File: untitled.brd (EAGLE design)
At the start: 43.2 x 14.4 mm, 38 parts, among them J2 1x3 RA Female .1", J3 CORTEX_DEBUG_PTH

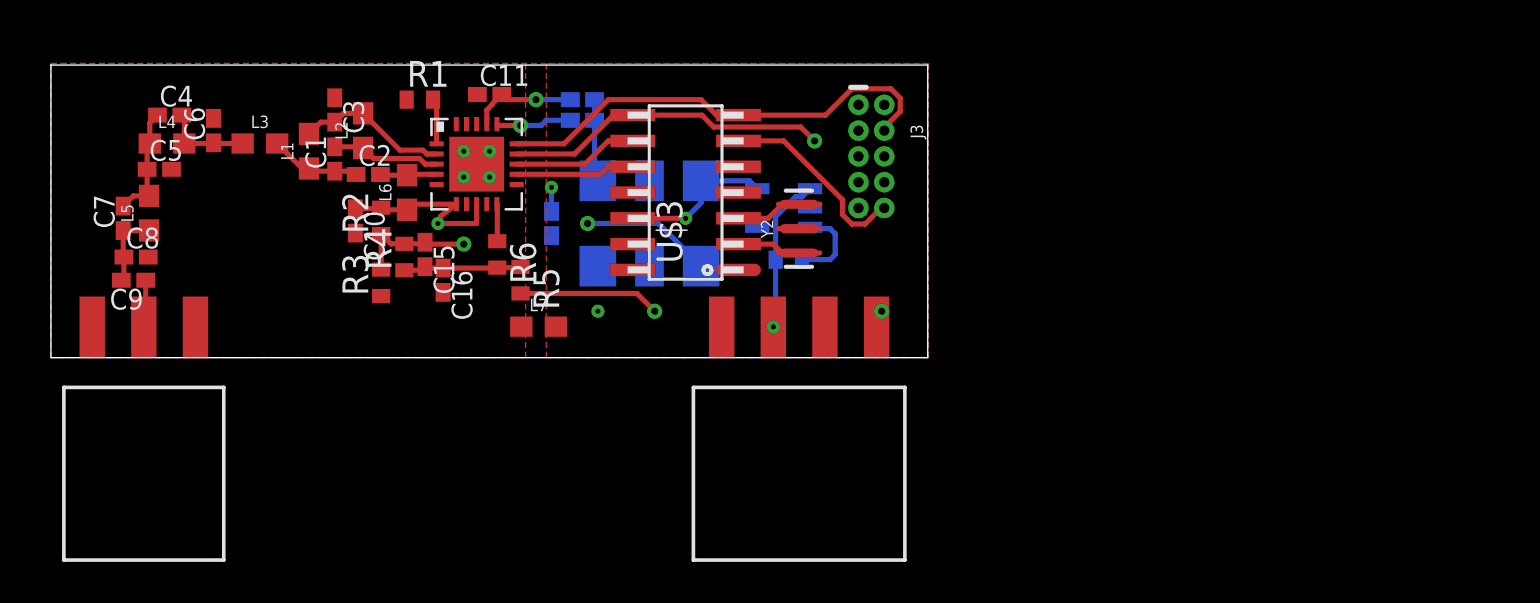
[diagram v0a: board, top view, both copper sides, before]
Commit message: Added USB connector
added USB connector for debugging, dropped to 4 layer board
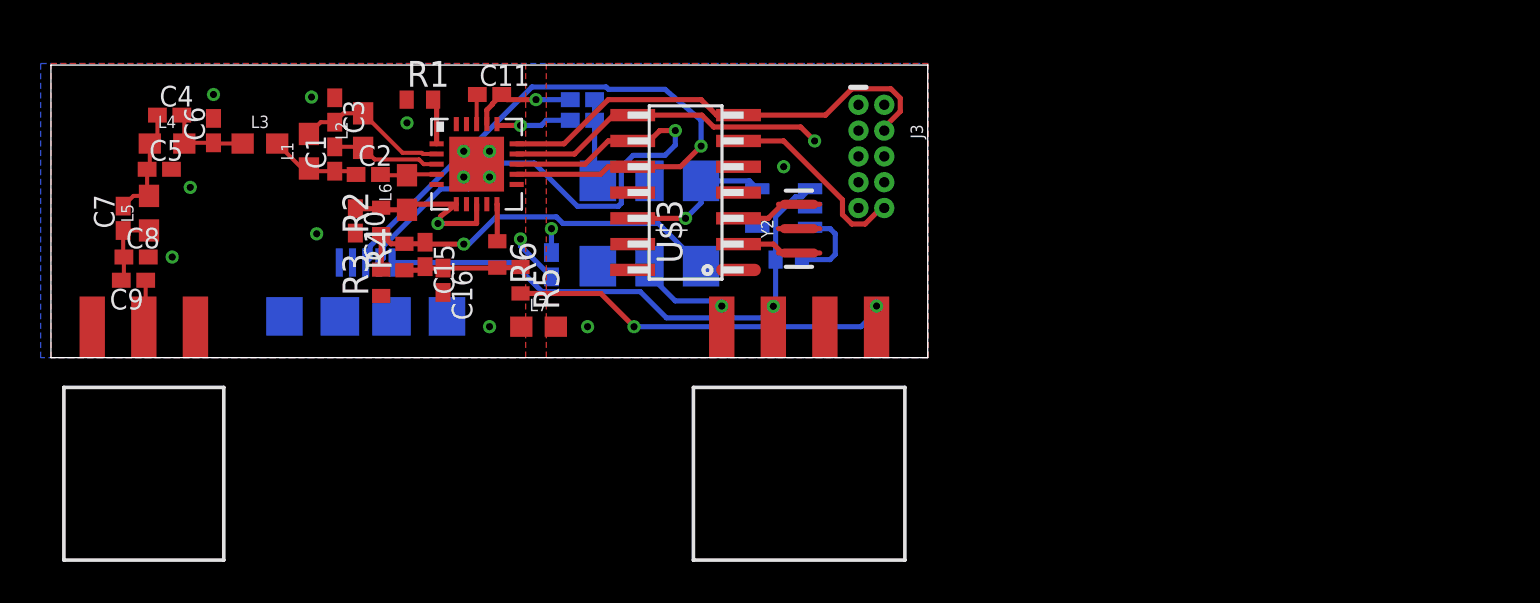
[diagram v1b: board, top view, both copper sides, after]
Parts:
- added J4: USB-MICROB, SparkFun-Retired:USB-MICROB
- moved C14 2.03 mm to (24.6, 4.57)
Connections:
- net 5V: now also J4.VBUS
- net GND: now also J4.GND, J4.MT1, J4.MT2
- net PA24: now also J4.D-
- net PA25: now also J4.D+
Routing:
- net PA25: track 5.87 -> 32.3 mm, vias 0 -> 1
- net PA24: track 6.19 -> 29.8 mm, vias 0 -> 1
- net 5V: track 8.62 -> 28.7 mm
- net ENABLE: track 0.00 -> 5.66 mm, vias 0 -> 1
- net GND: track 0.00 -> 4.87 mm, vias 5 -> 13
- net AUDIO: track 20.7 -> 19.8 mm
- net N$6: track 19.1 -> 19.3 mm, vias 2 -> 1
- net VCC: vias 3 -> 4
- added copper zone on layer 15, net VCC
- removed copper zone on layer 14, net VCC

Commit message: Added test points to SI4464
Added test points to unused pins for later use. Cleaned up routing.
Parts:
- added TP1, TP2, TP3, TP4, TP5: TEST-POINT3, SparkFun-Connectors:PAD.03X.03
- C1: value (none) -> 12pf
- C2: value (none) -> 470pf
- moved R6 1.27 mm to (22.0, 3.81)
- moved C11 0.76 mm to (22.4, 13.0)
- moved R1 0.65 mm to (17.5, 12.6), turned to 270 degrees
- moved R5 0.25 mm to (23.4, 3.81)
- moved L2 0.13 mm to (15.5, 11.2)
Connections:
- net GPIO0: now also TP2.P$1
- net GPIO2: now also TP4.P$1
- net GPIO3: now also TP5.P$1
- net NIRQ: now also TP3.P$1
- net TXRAMP: now also TP1.P$1
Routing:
- net GPIO0: track 0.00 -> 2.73 mm
- net NIRQ: track 0.00 -> 2.39 mm
- net N$6: track 19.3 -> 21.5 mm
- net GPIO3: track 0.00 -> 2.09 mm
- net 5V: track 28.7 -> 30.5 mm
- net N$4: track 5.84 -> 7.35 mm
- net GPIO2: track 0.00 -> 1.44 mm
- net MODULATION: track 1.83 -> 3.10 mm
- net TXRAMP: track 0.00 -> 1.26 mm
- net VCC: track 18.2 -> 19.2 mm
- net GND: track 4.87 -> 5.62 mm, vias 13 -> 12

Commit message: Added 0 ohm resistors to spi
added 0 ohm jumpers between spi pins on the micro and si4464
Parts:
- added R10, R11, R8, R9: 0, resistor:R0402
- moved TP3 2.17 mm to (25.9, 6.10)
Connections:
- new net PA241: R10.1, U$2.13
- new net PA251: R11.1, U$2.12
- new net SWDCLK1: R8.1, U$2.15
- new net SWDIO1: R9.1, U$2.14
- net PA24: now also R10.2; no longer U$2.13
- net PA25: now also R11.2; no longer U$2.12
- net SWDCLK: now also R8.2; no longer U$2.15
- net SWDIO: now also R9.2; no longer U$2.14
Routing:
- net SWDCLK: track 22.7 -> 19.1 mm
- net SWDIO: track 21.2 -> 17.9 mm
- net PA24: track 29.8 -> 26.9 mm
- net PA25: track 32.3 -> 29.8 mm
- net SWDCLK1: track 0.00 -> 2.31 mm
- net PA251: track 0.00 -> 2.30 mm
- net SWDIO1: track 0.00 -> 1.99 mm
- net PA241: track 0.00 -> 1.98 mm
- net NIRQ: track 2.39 -> 4.26 mm
- net VCC: vias 4 -> 3
- net GND: vias 12 -> 13
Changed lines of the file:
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@@
 <element name="TP1" library="SparkFun-Connectors" library_urn="urn:adsk.eagle:library:513" package="PAD.03X.03" package3d_urn="urn:adsk.eagle:package:38286/1" value="TEST-POINT3" x="20.32" y="6.35"/>
 <element name="TP2" library="SparkFun-Connectors" library_urn="urn:adsk.eagle:library:513" package="PAD.03X.03" package3d_urn="urn:adsk.eagle:package:38286/1" value="TEST-POINT3" x="20.828" y="5.08"/>
-<element name="TP3" library="SparkFun-Connectors" library_urn="urn:adsk.eagle:library:513" package="PAD.03X.03" package3d_urn="urn:adsk.eagle:package:38286/1" value="TEST-POINT3" x="25.146" y="8.128"/>
+<element name="TP3" library="SparkFun-Connectors" library_urn="urn:adsk.eagle:library:513" package="PAD.03X.03" package3d_urn="urn:adsk.eagle:package:38286/1" value="TEST-POINT3" x="25.908" y="6.096"/>
 <element name="TP4" library="SparkFun-Connectors" library_urn="urn:adsk.eagle:library:513" package="PAD.03X.03" package3d_urn="urn:adsk.eagle:package:38286/1" value="TEST-POINT3" x="20.193" y="12.827"/>
 <element name="TP5" library="SparkFun-Connectors" library_urn="urn:adsk.eagle:library:513" package="PAD.03X.03" package3d_urn="urn:adsk.eagle:package:38286/1" value="TEST-POINT3" x="19.05" y="13.208"/>
+<element name="R8" library="resistor" library_urn="urn:adsk.eagle:library:348" package="R0402" package3d_urn="urn:adsk.eagle:package:26058/1" value="0" x="25.4" y="11.684"/>
+<element name="R9" library="resistor" library_urn="urn:adsk.eagle:library:348" package="R0402" package3d_urn="urn:adsk.eagle:package:26058/1" value="0" x="25.4" y="10.414"/>
+<element name="R10" library="resistor" library_urn="urn:adsk.eagle:library:348" package="R0402" package3d_urn="urn:adsk.eagle:package:26058/1" value="0" x="25.4" y="9.144"/>
+<element name="R11" library="resistor" library_urn="urn:adsk.eagle:library:348" package="R0402" package3d_urn="urn:adsk.eagle:package:26058/1" value="0" x="25.4" y="7.874"/>
 </elements>
 <signals>
@@
 <wire x1="23.114" y1="5.496" x2="23.114" y2="5.842" width="0.254" layer="16"/>
 <wire x1="20.955" y1="9.525" x2="21.59" y2="8.89" width="0.254" layer="1"/>
+<via x="38.1" y="2.54" extent="1-16" drill="0.35" diameter="0.55"/>
 </signal>
 <signal name="RADIO_SDN">
@@
 <vertex x="0" y="0"/>
 </polygon>
-<via x="36.068" y="9.398" extent="1-16" drill="0.35"/>
 <wire x1="19.955" y1="7.555" x2="19.955" y2="7.509" width="0.254" layer="1"/>
 <wire x1="19.955" y1="7.509" x2="19.05" y2="6.604" width="0.254" layer="1"/>
@@
 <contactref element="U$2" pad="11"/>
 <contactref element="TP3" pad="P$1"/>
-<wire x1="22.925" y1="8.525" x2="24.749" y2="8.525" width="0.254" layer="1"/>
-<wire x1="24.749" y1="8.525" x2="25.146" y2="8.128" width="0.254" layer="1"/>
+<wire x1="22.925" y1="8.525" x2="23.876" y2="7.574" width="0.254" layer="1"/>
+<wire x1="23.876" y1="7.574" x2="23.876" y2="7.112" width="0.254" layer="1"/>
+<wire x1="23.876" y1="7.112" x2="24.0566" y2="6.9314" width="0.254" layer="1"/>
+<wire x1="25.714225" y1="6.096" x2="25.908" y2="6.096" width="0.254" layer="1"/>
+<wire x1="24.0566" y1="6.9314" x2="24.878825" y2="6.9314" width="0.254" layer="1"/>
+<wire x1="24.878825" y1="6.9314" x2="25.714225" y2="6.096" width="0.254" layer="1"/>
 </signal>
 <signal name="TXRAMP">
@@
 <contactref element="J3" pad="2"/>
 <contactref element="U$3" pad="8"/>
-<contactref element="U$2" pad="14"/>
-<wire x1="22.925" y1="10.025" x2="25.773" y2="10.025" width="0.254" layer="1"/>
-<wire x1="25.773" y1="10.025" x2="27.686" y2="11.938" width="0.254" layer="1"/>
-<wire x1="27.686" y1="11.938" x2="28.6385" y2="11.938" width="0.254" layer="1"/>
+<wire x1="28.6385" y1="11.938" x2="27.686" y2="11.938" width="0.254" layer="1"/>
 <wire x1="28.6385" y1="11.938" x2="32.04066875" y2="11.938" width="0.254" layer="1"/>
 <wire x1="36.9062" y1="11.3538" x2="37.592" y2="10.668" width="0.254" layer="1"/>
@@
 <wire x1="38.9636" y1="12.0396" x2="38.9636" y2="12.77215625" width="0.254" layer="15"/>
 <wire x1="40.07715625" y1="13.2334" x2="40.86455625" y2="12.446" width="0.254" layer="15"/>
+<contactref element="R9" pad="2"/>
+<wire x1="27.686" y1="11.938" x2="26.162" y2="10.414" width="0.254" layer="1"/>
+<wire x1="26.162" y1="10.414" x2="26.05" y2="10.414" width="0.254" layer="1"/>
 </signal>
 <signal name="KEY">
@@
 <contactref element="J3" pad="4"/>
 <contactref element="U$3" pad="7"/>
-<contactref element="U$2" pad="15"/>
-<wire x1="22.925" y1="10.525" x2="25.257" y2="10.525" width="0.254" layer="1"/>
-<wire x1="25.257" y1="10.525" x2="27.432" y2="12.7" width="0.254" layer="1"/>
-<wire x1="27.432" y1="12.7" x2="32.004" y2="12.7" width="0.254" layer="1"/>
+<wire x1="32.004" y1="12.7" x2="27.432" y2="12.7" width="0.254" layer="1"/>
 <wire x1="32.004" y1="12.7" x2="32.766" y2="11.938" width="0.254" layer="1"/>
 <wire x1="32.766" y1="11.938" x2="33.8455" y2="11.938" width="0.254" layer="1"/>
@@
 <wire x1="41.021" y1="11.33244375" x2="41.021" y2="11.176" width="0.254" layer="1"/>
 <wire x1="41.8084" y1="12.11984375" x2="41.021" y2="11.33244375" width="0.254" layer="1"/>
+<contactref element="R8" pad="2"/>
+<wire x1="27.432" y1="12.7" x2="27.066" y2="12.7" width="0.254" layer="1"/>
+<wire x1="27.066" y1="12.7" x2="26.05" y2="11.684" width="0.254" layer="1"/>
 </signal>
 <signal name="N$17">
@@
 <signal name="PA25">
 <contactref element="U$3" pad="10"/>
-<contactref element="U$2" pad="12"/>
-<wire x1="22.925" y1="9.025" x2="27.059" y2="9.025" width="0.254" layer="1"/>
 <wire x1="27.059" y1="9.025" x2="27.432" y2="9.398" width="0.254" layer="1"/>
 <wire x1="27.432" y1="9.398" x2="28.6385" y2="9.398" width="0.254" layer="1"/>
@@
 <wire x1="32.004" y1="10.414" x2="30.988" y2="9.398" width="0.254" layer="1"/>
 <wire x1="30.988" y1="9.398" x2="28.6385" y2="9.398" width="0.254" layer="1"/>
+<contactref element="R11" pad="2"/>
+<wire x1="26.05" y1="7.874" x2="27.059" y2="8.883" width="0.254" layer="1"/>
+<wire x1="27.059" y1="8.883" x2="27.059" y2="9.025" width="0.254" layer="1"/>
 </signal>
 <signal name="PA24">
 <contactref element="U$3" pad="9"/>
-<contactref element="U$2" pad="13"/>
-<wire x1="22.925" y1="9.525" x2="26.289" y2="9.525" width="0.254" layer="1"/>
-<wire x1="26.289" y1="9.525" x2="27.432" y2="10.668" width="0.254" layer="1"/>
-<wire x1="27.432" y1="10.668" x2="28.6385" y2="10.668" width="0.254" layer="1"/>
+<wire x1="28.6385" y1="10.668" x2="27.432" y2="10.668" width="0.254" layer="1"/>
 <contactref element="J4" pad="D-"/>
 <wire x1="16.144" y1="4.682" x2="16.365" y2="4.903" width="0.254" layer="16"/>
@@
 <wire x1="29.972" y1="11.176" x2="29.464" y2="10.668" width="0.254" layer="1"/>
 <wire x1="29.464" y1="10.668" x2="28.6385" y2="10.668" width="0.254" layer="1"/>
+<contactref element="R10" pad="2"/>
+<wire x1="27.432" y1="10.668" x2="26.654" y2="9.89" width="0.254" layer="1"/>
+<wire x1="26.654" y1="9.89" x2="26.654" y2="9.8587875" width="0.254" layer="1"/>
+<wire x1="26.05" y1="9.2547875" x2="26.05" y2="9.144" width="0.254" layer="1"/>
+<wire x1="26.654" y1="9.8587875" x2="26.05" y2="9.2547875" width="0.254" layer="1"/>
 </signal>
 <signal name="5V">
@@
 <contactref element="U$4" pad="4"/>
 </signal>
+<signal name="SWDCLK1">
+<contactref element="U$2" pad="15"/>
+<contactref element="R8" pad="1"/>
+<wire x1="24.75" y1="11.684" x2="23.5816" y2="10.5156" width="0.254" layer="1"/>
+<wire x1="22.9344" y1="10.5156" x2="22.925" y2="10.525" width="0.254" layer="1"/>
+<wire x1="23.5816" y1="10.5156" x2="22.9344" y2="10.5156" width="0.254" layer="1"/>
+</signal>
+<signal name="SWDIO1">
+<contactref element="U$2" pad="14"/>
+<contactref element="R9" pad="1"/>
+<wire x1="24.75" y1="10.414" x2="24.13" y2="10.414" width="0.254" layer="1"/>
+<wire x1="23.741" y1="10.025" x2="22.925" y2="10.025" width="0.254" layer="1"/>
+<wire x1="24.13" y1="10.414" x2="23.741" y2="10.025" width="0.254" layer="1"/>
+</signal>
+<signal name="PA241">
+<contactref element="U$2" pad="13"/>
+<contactref element="R10" pad="1"/>
+<wire x1="22.925" y1="9.525" x2="23.749" y2="9.525" width="0.254" layer="1"/>
+<wire x1="23.749" y1="9.525" x2="24.13" y2="9.144" width="0.254" layer="1"/>
+<wire x1="24.13" y1="9.144" x2="24.75" y2="9.144" width="0.254" layer="1"/>
+</signal>
+<signal name="PA251">
+<contactref element="U$2" pad="12"/>
+<contactref element="R11" pad="1"/>
+<wire x1="22.925" y1="9.025" x2="23.599" y2="9.025" width="0.254" layer="1"/>
+<wire x1="23.599" y1="9.025" x2="24.75" y2="7.874" width="0.254" layer="1"/>
+</signal>
 </signals>

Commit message: changed audio input path
changed audio input to make the samd11c14 decode the audio and resend it to the VCO. Added fets to allow for i2c over enable and audio pins for future use.
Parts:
- removed TP3: TEST-POINT3, SparkFun-Connectors:PAD.03X.03
- removed Y2: (no value), SparkFun-Clocks:RESONATOR-SMD-3.2X1.3
- added Q1, Q2: BSS123, transistor-small-signal:SOT23
- added R12, R14: 10k, resistor:R0402
- added R13, R15: 20k, resistor:R0402
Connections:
- removed net MXIN: U$3.2, Y2.1
- removed net MXOUT: U$3.3, Y2.3
- removed net NIRQ: TP3.P$1, U$2.11
- removed net PA05: U$3.1
- removed net PA15: U$3.5
- new net AUDIO_IO: J1.4, R12.1, R13.2, U$3.5
- new net N$7: Q1.3, R13.1
- new net N$8: Q2.3, R15.1
- new net PA08: U$3.2
- net AUDIO: now also R12.2, U$3.1; no longer J1.4
- net ENABLE: now also R14.2
- net GND: now also Q1.2, Q2.2; no longer Y2.2
- net MODULATION: now also U$3.3
- net PA02: now also U$2.11
- net PA04: now also Q1.1, Q2.1
- net PA14: now also R14.1, R15.2
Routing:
- net MODULATION: track 3.10 -> 16.0 mm
- net AUDIO: track 19.5 -> 11.0 mm, vias 2 -> 0
- net PA02: track 0.00 -> 6.93 mm
- net NIRQ: track 4.26 -> 0.00 mm
- net MXOUT: track 3.27 -> 0.00 mm
- net MXIN: track 3.17 -> 0.00 mm
- added copper zone on layer 2, net N$10
